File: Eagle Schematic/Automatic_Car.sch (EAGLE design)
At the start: 15 parts, among them M1 MOTOR10MM, M2 MOTOR10MM, U1 GY-521MPU6050

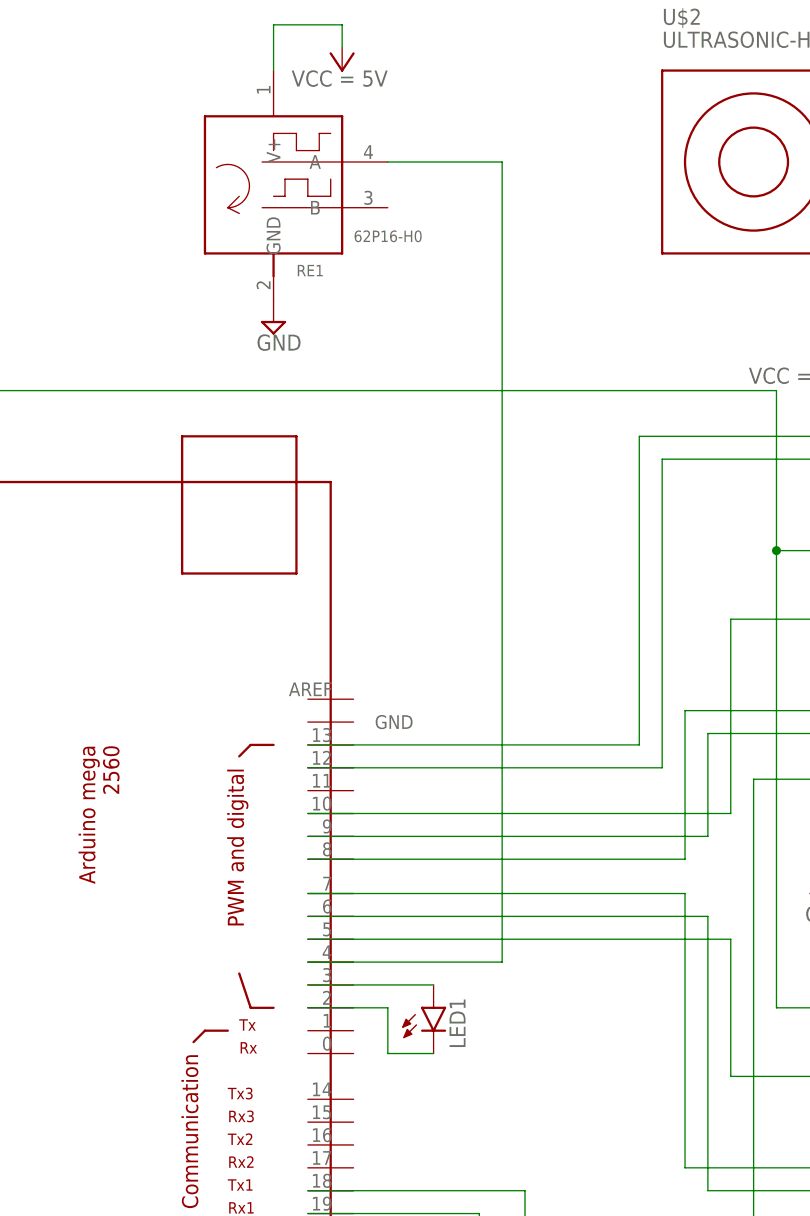
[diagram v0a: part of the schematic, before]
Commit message: Encoder is active
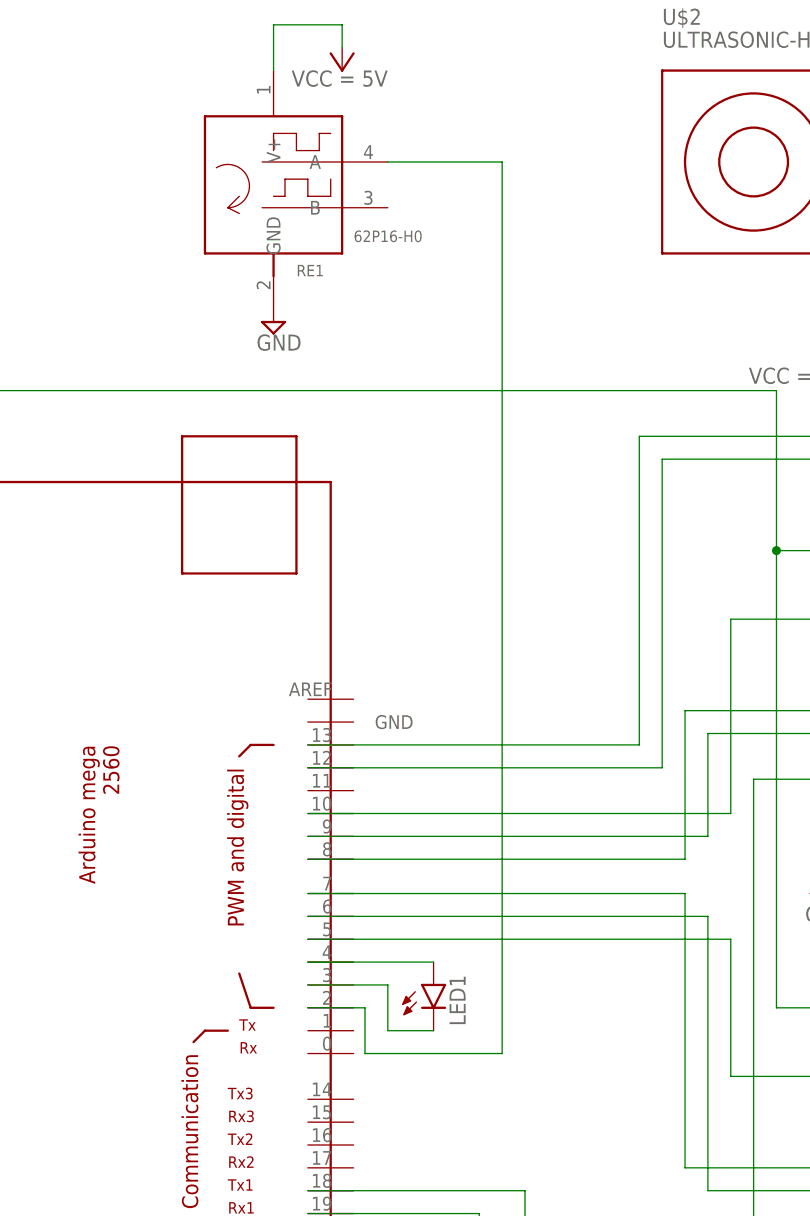
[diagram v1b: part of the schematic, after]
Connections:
- net N$18: now also U$1.4; no longer U$1.3
- net N$21: now also U$1.3; no longer U$1.2
- net N$22: now also U$1.2; no longer U$1.4
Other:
- moved on the sheet: LED1
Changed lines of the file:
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@@
 <attribute name="VCC" x="-35.56" y="27.94" size="1.778" layer="96" display="both"/>
 </instance>
-<instance part="LED1" gate="G$1" x="38.1" y="-7.62" smashed="yes">
-<attribute name="NAME" x="41.656" y="-12.192" size="1.778" layer="95" rot="R90"/>
+<instance part="LED1" gate="G$1" x="38.1" y="-5.08" smashed="yes">
+<attribute name="NAME" x="41.656" y="-9.652" size="1.778" layer="95" rot="R90"/>
 </instance>
 <instance part="RE1" gate="G$1" x="20.32" y="83.82" smashed="yes">
@@
 </segment>
 </net>
-<net name="N$18" class="0">
-<segment>
-<pinref part="U$1" gate="G$1" pin="3"/>
-<pinref part="LED1" gate="G$1" pin="A"/>
-<wire x1="24.13" y1="-5.08" x2="38.1" y2="-5.08" width="0.1524" layer="91"/>
-</segment>
-</net>
-<net name="N$21" class="0">
-<segment>
-<pinref part="U$1" gate="G$1" pin="2"/>
-<wire x1="24.13" y1="-7.62" x2="33.02" y2="-7.62" width="0.1524" layer="91"/>
-<wire x1="33.02" y1="-7.62" x2="33.02" y2="-12.7" width="0.1524" layer="91"/>
-<pinref part="LED1" gate="G$1" pin="C"/>
-<wire x1="33.02" y1="-12.7" x2="38.1" y2="-12.7" width="0.1524" layer="91"/>
-</segment>
-</net>
 <net name="N$22" class="0">
 <segment>
 <pinref part="RE1" gate="G$1" pin="A"/>
 <wire x1="33.02" y1="86.36" x2="45.72" y2="86.36" width="0.1524" layer="91"/>
-<wire x1="45.72" y1="86.36" x2="45.72" y2="-2.54" width="0.1524" layer="91"/>
+<wire x1="45.72" y1="86.36" x2="45.72" y2="-12.7" width="0.1524" layer="91"/>
+<wire x1="45.72" y1="-12.7" x2="30.48" y2="-12.7" width="0.1524" layer="91"/>
+<wire x1="30.48" y1="-12.7" x2="30.48" y2="-7.62" width="0.1524" layer="91"/>
+<pinref part="U$1" gate="G$1" pin="2"/>
+<wire x1="30.48" y1="-7.62" x2="24.13" y2="-7.62" width="0.1524" layer="91"/>
+</segment>
+</net>
+<net name="N$18" class="0">
+<segment>
+<pinref part="LED1" gate="G$1" pin="A"/>
 <pinref part="U$1" gate="G$1" pin="4"/>
-<wire x1="45.72" y1="-2.54" x2="24.13" y2="-2.54" width="0.1524" layer="91"/>
-</segment>
-</net>
+<wire x1="38.1" y1="-2.54" x2="24.13" y2="-2.54" width="0.1524" layer="91"/>
+</segment>
+</net>
+<net name="N$21" class="0">
+<segment>
+<pinref part="LED1" gate="G$1" pin="C"/>
+<wire x1="38.1" y1="-10.16" x2="33.02" y2="-10.16" width="0.1524" layer="91"/>
+<wire x1="33.02" y1="-10.16" x2="33.02" y2="-5.08" width="0.1524" layer="91"/>
+<pinref part="U$1" gate="G$1" pin="3"/>
+<wire x1="33.02" y1="-5.08" x2="24.13" y2="-5.08" width="0.1524" layer="91"/>
+</segment>
+</net>
